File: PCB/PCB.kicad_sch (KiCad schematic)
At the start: 17 parts, among them J1 Conn_01x06_Female, J2 09252306841, U13 74HC165, U15 LT3042xMSE, U16 74HC165

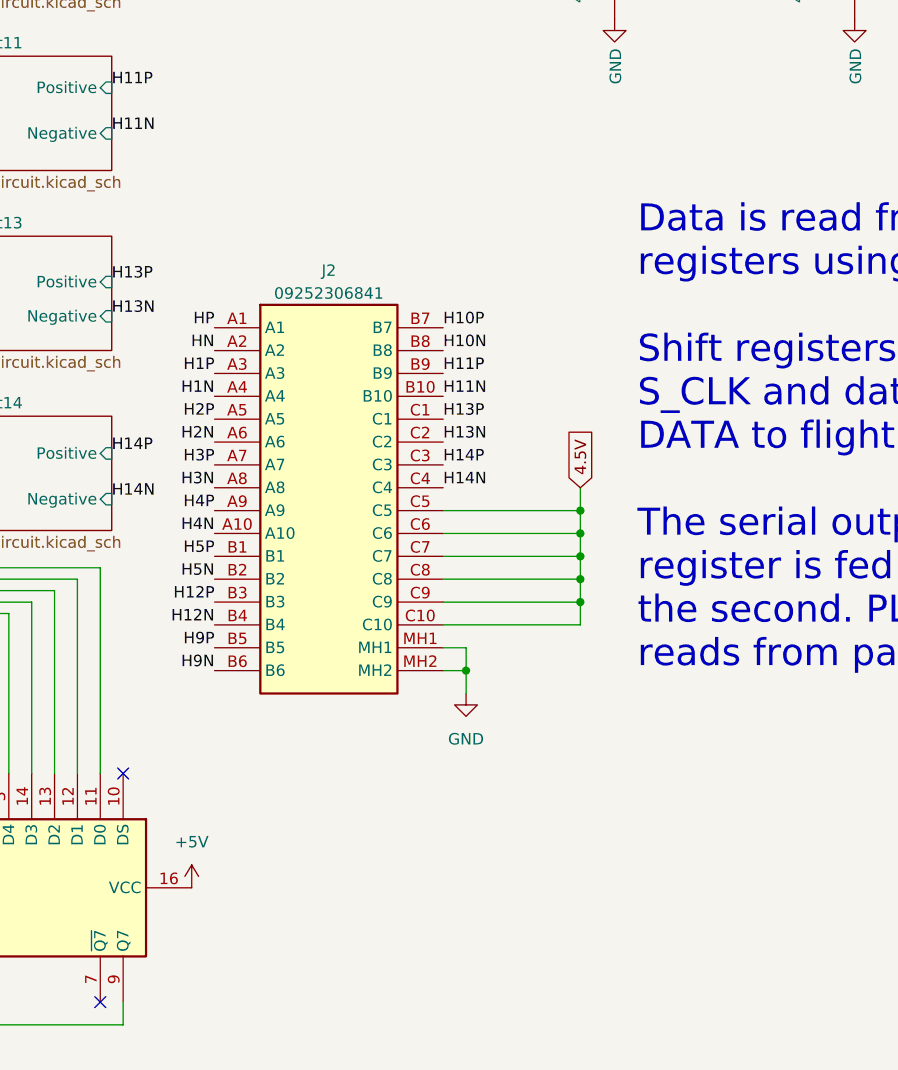
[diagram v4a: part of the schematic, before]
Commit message: Connector update
Changed the connector I found to a db25 and adjusted the radius of components to compensate
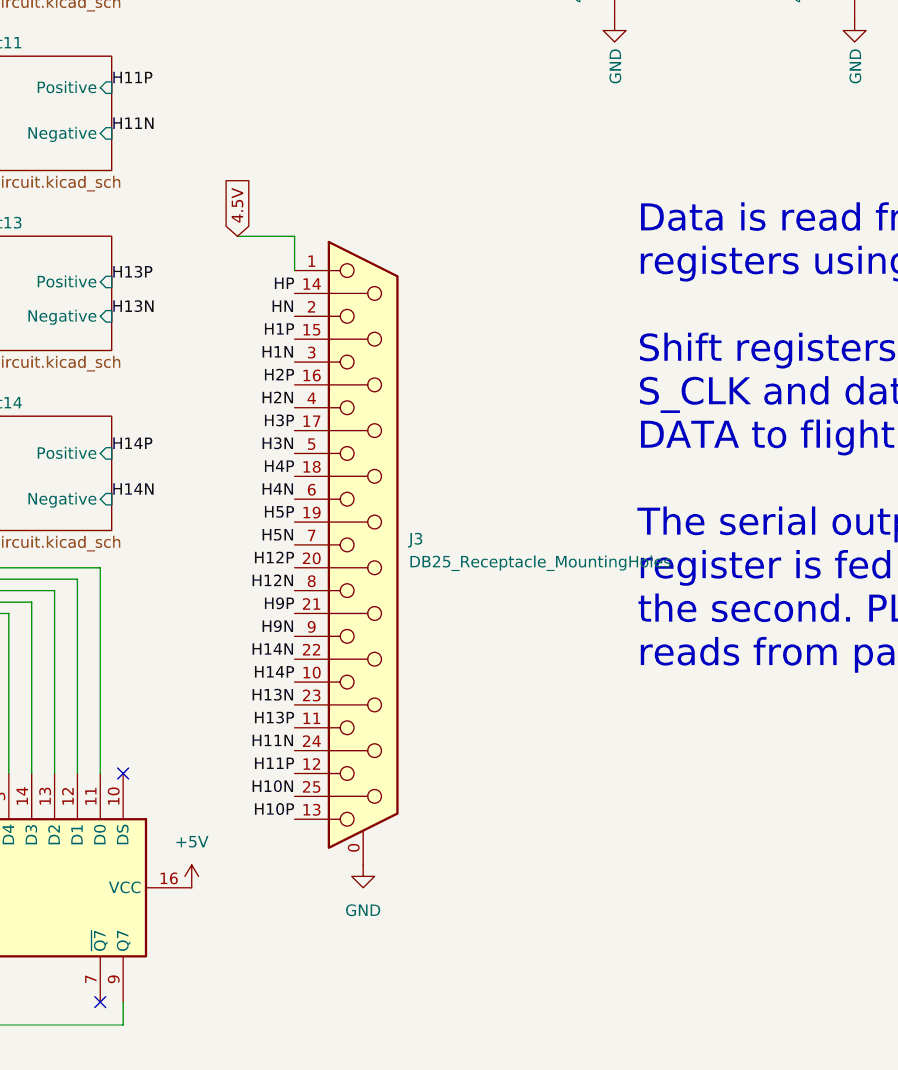
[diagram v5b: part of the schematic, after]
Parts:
- removed J2: 09252306841, 09252306841:09252306841, symbol 09252306841:09252306841
- added J3: DB25_Receptacle_MountingHoles, Connector_Dsub:DSUB-25_Female_Vertical_P2.77x2.84mm_MountingHoles, symbol Connector:DB25_Receptacle_MountingHoles
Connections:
- net 4.5V: now also J3.1
- net GND: now also J3.0 (PAD)
- net H10N: now also J3.25 (P25)
- net H10P: now also J3.13
- net H11N: now also J3.24 (P24)
- net H11P: now also J3.12
- net H12N: now also J3.8
- net H12P: now also J3.20 (P20)
- net H13N: now also J3.23 (P23)
- net H13P: now also J3.11
- net H14N: now also J3.22 (P22)
- net H14P: now also J3.10
- net H1N: now also J3.3
- net H1P: now also J3.15 (P15)
- net H2N: now also J3.4
- net H2P: now also J3.16 (P16)
- net H3N: now also J3.5
- net H3P: now also J3.17 (P17)
- net H4N: now also J3.6
- net H4P: now also J3.18 (P18)
- net H5N: now also J3.7
- net H5P: now also J3.19 (P19)
- net H9N: now also J3.9
- net H9P: now also J3.21 (P21)
- net HN: now also J3.2
- net HP: now also J3.14 (P14)

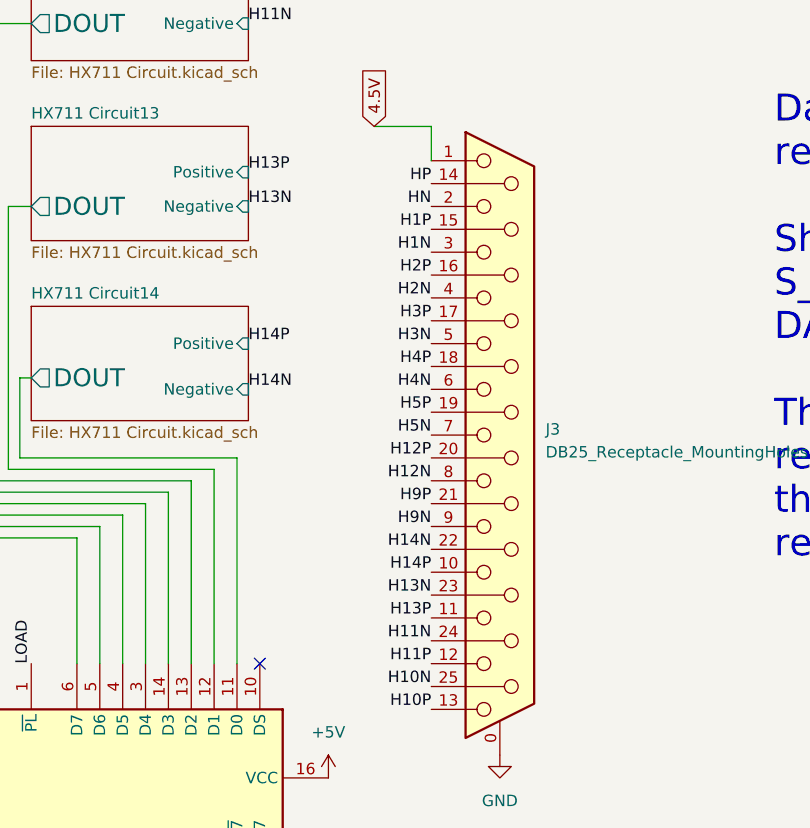
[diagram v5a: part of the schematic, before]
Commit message: updated PCB
Current version with errors
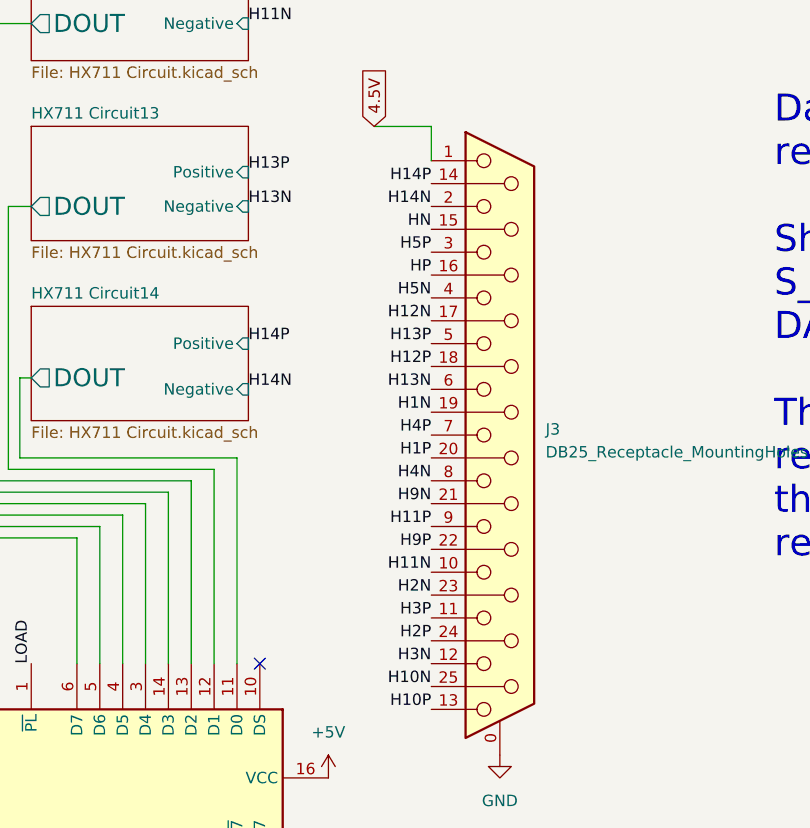
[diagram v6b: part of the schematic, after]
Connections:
- net H11N: now also J3.10; no longer J3.24 (P24)
- net H11P: now also J3.9; no longer J3.12
- net H12N: now also J3.17 (P17); no longer J3.8
- net H12P: now also J3.18 (P18); no longer J3.20 (P20)
- net H13N: now also J3.6; no longer J3.23 (P23)
- net H13P: now also J3.5; no longer J3.11
- net H14N: now also J3.2; no longer J3.22 (P22)
- net H14P: now also J3.14 (P14); no longer J3.10
- net H1N: now also J3.19 (P19); no longer J3.3
- net H1P: now also J3.20 (P20); no longer J3.15 (P15)
- net H2N: now also J3.23 (P23); no longer J3.4
- net H2P: now also J3.24 (P24); no longer J3.16 (P16)
- net H3N: now also J3.12; no longer J3.5
- net H3P: now also J3.11; no longer J3.17 (P17)
- net H4N: now also J3.8; no longer J3.6
- net H4P: now also J3.7; no longer J3.18 (P18)
- net H5N: now also J3.4; no longer J3.7
- net H5P: now also J3.3; no longer J3.19 (P19)
- net H9N: now also J3.21 (P21); no longer J3.9
- net H9P: now also J3.22 (P22); no longer J3.21 (P21)
- net HN: now also J3.15 (P15); no longer J3.2
- net HP: now also J3.16 (P16); no longer J3.14 (P14)
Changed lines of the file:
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@@
-    (effects (font (size 1.27 1.27)) (justify right bottom))
-  )
-  (label "H9N" (at 133.35 149.86 180) (fields_autoplaced)
-    (effects (font (size 1.27 1.27)) (justify right bottom))
-  )
-  (label "H10P" (at 133.35 170.18 180) (fields_autoplaced)
     (effects (font (size 1.27 1.27)) (justify right bottom))
   )
@@
     (effects (font (size 1.27 1.27)) (justify left bottom))
   )
-  (label "H1P" (at 133.35 116.84 180) (fields_autoplaced)
-    (effects (font (size 1.27 1.27)) (justify right bottom))
-  )
-  (label "H3P" (at 133.35 127 180) (fields_autoplaced)
-    (effects (font (size 1.27 1.27)) (justify right bottom))
-  )
-  (label "H12N" (at 133.35 144.78 180) (fields_autoplaced)
+  (label "H2P" (at 133.35 162.56 180) (fields_autoplaced)
     (effects (font (size 1.27 1.27)) (justify right bottom))
   )
@@
     (effects (font (size 1.27 1.27)) (justify left bottom))
   )
-  (label "HN" (at 133.35 114.3 180) (fields_autoplaced)
+  (label "H12P" (at 133.35 132.08 180) (fields_autoplaced)
+    (effects (font (size 1.27 1.27)) (justify right bottom))
+  )
+  (label "H13P" (at 133.35 129.54 180) (fields_autoplaced)
+    (effects (font (size 1.27 1.27)) (justify right bottom))
+  )
+  (label "H10P" (at 133.35 170.18 180) (fields_autoplaced)
     (effects (font (size 1.27 1.27)) (justify right bottom))
   )
@@
     (effects (font (size 1.27 1.27)) (justify left bottom))
   )
-  (label "H11N" (at 133.35 162.56 180) (fields_autoplaced)
+  (label "H2N" (at 133.35 157.48 180) (fields_autoplaced)
     (effects (font (size 1.27 1.27)) (justify right bottom))
   )
-  (label "H5P" (at 133.35 137.16 180) (fields_autoplaced)
-    (effects (font (size 1.27 1.27)) (justify right bottom))
-  )
-  (label "H4N" (at 133.35 134.62 180) (fields_autoplaced)
-    (effects (font (size 1.27 1.27)) (justify right bottom))
-  )
-  (label "H2N" (at 133.35 124.46 180) (fields_autoplaced)
-    (effects (font (size 1.27 1.27)) (justify right bottom))
-  )
-  (label "H11P" (at 133.35 165.1 180) (fields_autoplaced)
+  (label "H14P" (at 133.35 111.76 180) (fields_autoplaced)
     (effects (font (size 1.27 1.27)) (justify right bottom))
   )
@@
   (label "H9P" (at 113.03 50.8 0) (fields_autoplaced)
     (effects (font (size 1.27 1.27)) (justify left bottom))
+  )
+  (label "H13N" (at 133.35 134.62 180) (fields_autoplaced)
+    (effects (font (size 1.27 1.27)) (justify right bottom))
   )
   (label "LOAD" (at 251.46 31.75 180) (fields_autoplaced)
@@
     (effects (font (size 1.27 1.27)) (justify left bottom))
   )
-  (label "H4P" (at 133.35 132.08 180) (fields_autoplaced)
+  (label "H3N" (at 133.35 165.1 180) (fields_autoplaced)
     (effects (font (size 1.27 1.27)) (justify right bottom))
   )
@@
     (effects (font (size 1.27 1.27)) (justify left bottom))
   )
-  (label "H14P" (at 133.35 154.94 180) (fields_autoplaced)
-    (effects (font (size 1.27 1.27)) (justify right bottom))
-  )
   (label "H11P" (at 113.03 88.9 0) (fields_autoplaced)
     (effects (font (size 1.27 1.27)) (justify left bottom))
   )
-  (label "H2P" (at 133.35 121.92 180) (fields_autoplaced)
+  (label "H9N" (at 133.35 147.32 180) (fields_autoplaced)
+    (effects (font (size 1.27 1.27)) (justify right bottom))
+  )
+  (label "HP" (at 133.35 121.92 180) (fields_autoplaced)
     (effects (font (size 1.27 1.27)) (justify right bottom))
   )
@@
     (effects (font (size 1.27 1.27)) (justify right bottom))
   )
-  (label "H14N" (at 133.35 152.4 180) (fields_autoplaced)
-    (effects (font (size 1.27 1.27)) (justify right bottom))
-  )
   (label "H2P" (at 34.29 71.12 180) (fields_autoplaced)
     (effects (font (size 1.27 1.27)) (justify right bottom))
@@
     (effects (font (size 1.27 1.27)) (justify right bottom))
   )
-  (label "H9P" (at 133.35 147.32 180) (fields_autoplaced)
+  (label "H4P" (at 133.35 139.7 180) (fields_autoplaced)
+    (effects (font (size 1.27 1.27)) (justify right bottom))
+  )
+  (label "H4N" (at 133.35 144.78 180) (fields_autoplaced)
+    (effects (font (size 1.27 1.27)) (justify right bottom))
+  )
+  (label "HN" (at 133.35 116.84 180) (fields_autoplaced)
     (effects (font (size 1.27 1.27)) (justify right bottom))
   )
@@
     (effects (font (size 1.27 1.27)) (justify right bottom))
   )
-  (label "H1N" (at 133.35 119.38 180) (fields_autoplaced)
+  (label "DATA" (at 251.46 29.21 180) (fields_autoplaced)
     (effects (font (size 1.27 1.27)) (justify right bottom))
   )
-  (label "DATA" (at 251.46 29.21 180) (fields_autoplaced)
+  (label "H1N" (at 133.35 137.16 180) (fields_autoplaced)
+    (effects (font (size 1.27 1.27)) (justify right bottom))
+  )
+  (label "H11N" (at 133.35 154.94 180) (fields_autoplaced)
     (effects (font (size 1.27 1.27)) (justify right bottom))
   )
@@
     (effects (font (size 1.27 1.27)) (justify right bottom))
   )
-  (label "H3N" (at 133.35 129.54 180) (fields_autoplaced)
+  (label "H11P" (at 133.35 149.86 180) (fields_autoplaced)
+    (effects (font (size 1.27 1.27)) (justify right bottom))
+  )
+  (label "H12N" (at 133.35 127 180) (fields_autoplaced)
+    (effects (font (size 1.27 1.27)) (justify right bottom))
+  )
+  (label "H3P" (at 133.35 160.02 180) (fields_autoplaced)
+    (effects (font (size 1.27 1.27)) (justify right bottom))
+  )
+  (label "H9P" (at 133.35 152.4 180) (fields_autoplaced)
     (effects (font (size 1.27 1.27)) (justify right bottom))
   )
@@
     (effects (font (size 1.27 1.27)) (justify right bottom))
   )
+  (label "H5N" (at 133.35 124.46 180) (fields_autoplaced)
+    (effects (font (size 1.27 1.27)) (justify right bottom))
+  )
   (label "H13N" (at 113.03 114.3 0) (fields_autoplaced)
     (effects (font (size 1.27 1.27)) (justify left bottom))
-  )
-  (label "HP" (at 133.35 111.76 180) (fields_autoplaced)
-    (effects (font (size 1.27 1.27)) (justify right bottom))
   )
   (label "H14P" (at 113.03 129.54 0) (fields_autoplaced)
@@
     (effects (font (size 1.27 1.27)) (justify left bottom))
   )
-  (label "H5N" (at 133.35 139.7 180) (fields_autoplaced)
+  (label "H9N" (at 113.03 55.88 0) (fields_autoplaced)
+    (effects (font (size 1.27 1.27)) (justify left bottom))
+  )
+  (label "H5P" (at 133.35 119.38 180) (fields_autoplaced)
     (effects (font (size 1.27 1.27)) (justify right bottom))
   )
-  (label "H9N" (at 113.03 55.88 0) (fields_autoplaced)
-    (effects (font (size 1.27 1.27)) (justify left bottom))
+  (label "H14N" (at 133.35 114.3 180) (fields_autoplaced)
+    (effects (font (size 1.27 1.27)) (justify right bottom))
   )
   (label "H2N" (at 34.29 74.93 180) (fields_autoplaced)
@@
     (effects (font (size 1.27 1.27)) (justify left bottom))
   )
+  (label "H1P" (at 133.35 142.24 180) (fields_autoplaced)
+    (effects (font (size 1.27 1.27)) (justify right bottom))
+  )
   (label "H12N" (at 113.03 34.29 0) (fields_autoplaced)
     (effects (font (size 1.27 1.27)) (justify left bottom))
   )
-  (label "H13P" (at 133.35 160.02 180) (fields_autoplaced)
-    (effects (font (size 1.27 1.27)) (justify right bottom))
-  )
-  (label "H12P" (at 133.35 142.24 180) (fields_autoplaced)
-    (effects (font (size 1.27 1.27)) (justify right bottom))
-  )
-  (label "H13N" (at 133.35 157.48 180) (fields_autoplaced)
-    (effects (font (size 1.27 1.27)) (justify right bottom))
-  )
   (global_label "4.5V" (shape input) (at 127 105.41 90) (fields_autoplaced)
